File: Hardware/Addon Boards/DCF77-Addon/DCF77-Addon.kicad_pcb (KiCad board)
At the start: 2 copper layers, 79 x 40.3 mm, 11 parts, among them J1 EXT, J4 EXT, J5 I2C_ext, J6 Prog, J8 GND, SW1 RST, SW2 SW_Plus, SW3 SW_Menu, SW4 SW_Minus

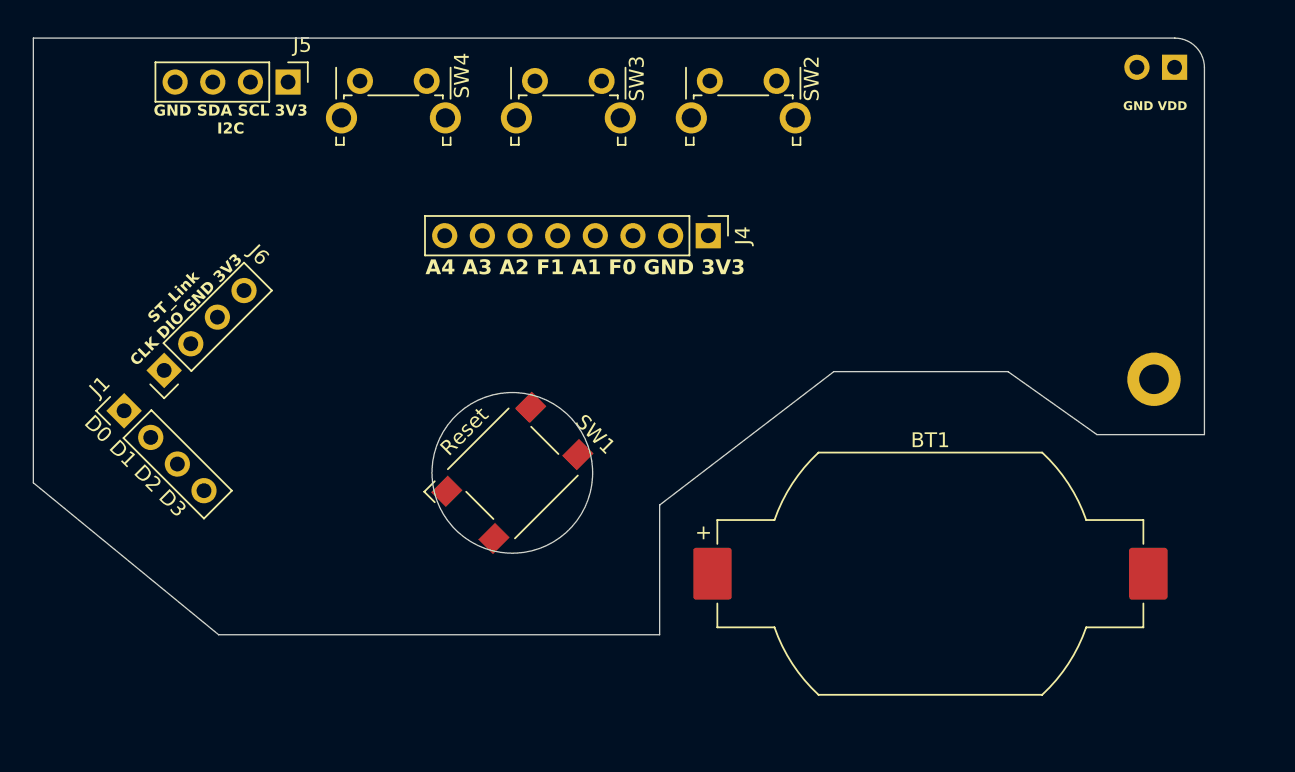
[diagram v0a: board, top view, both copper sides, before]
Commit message: Version bump 2.2.0 -> new regulator and id system
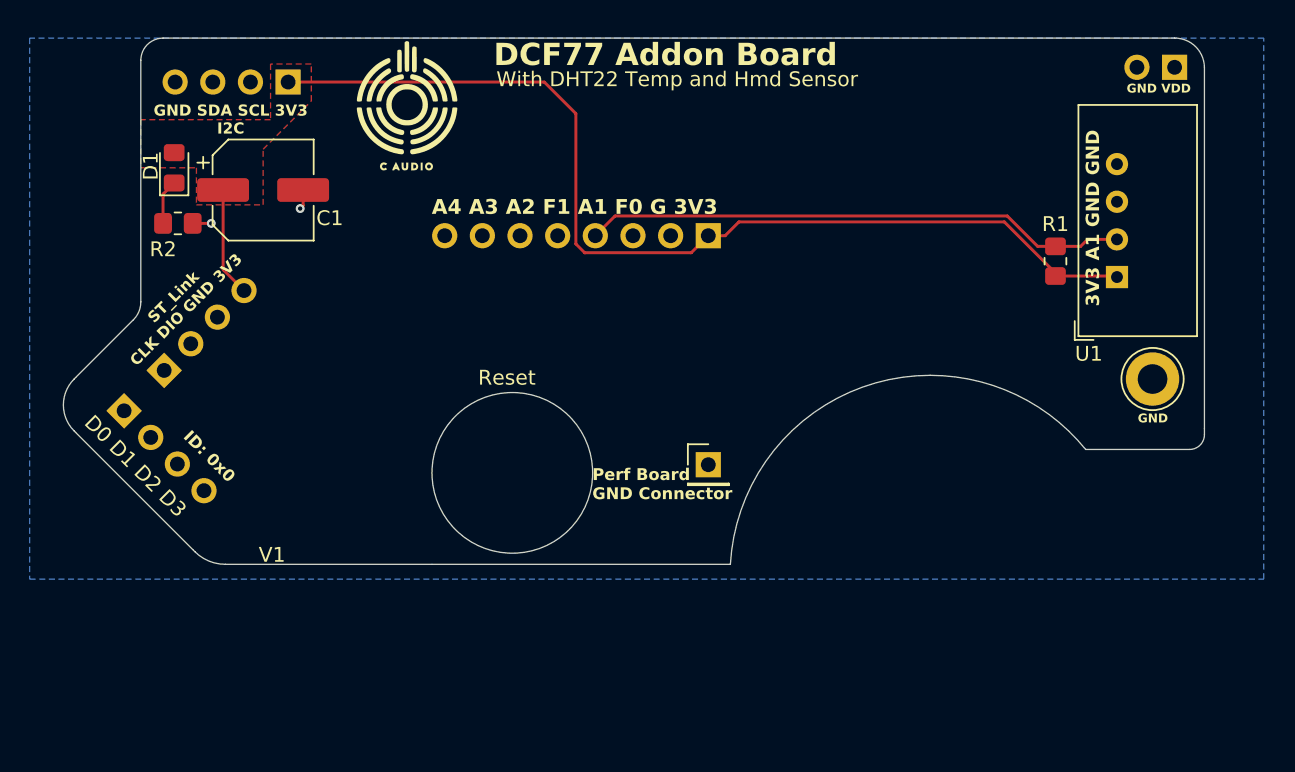
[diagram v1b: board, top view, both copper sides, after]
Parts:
- removed ?: , 
- removed BT1: Coin Cell, Battery:BatteryHolder_Renata_SMTU2032-LF_1x2032
- removed SW1: RST, Button_Switch_SMD:SW_SPST_Omron_B3FS-100xP
- removed SW2: SW_Plus, Button_Switch_THT:SW_Tactile_SPST_Angled_PTS645Vx31-2LFS
- removed SW3: SW_Menu, Button_Switch_THT:SW_Tactile_SPST_Angled_PTS645Vx31-2LFS
- removed SW4: SW_Minus, Button_Switch_THT:SW_Tactile_SPST_Angled_PTS645Vx31-2LFS
- added C1: 100u 16V, Capacitor_SMD:CP_Elec_6.3x7.7, F.Cu at (155.8, 62.8)
- added D1: LED_grn, LED_SMD:LED_0805_2012Metric_Pad1.15x1.40mm_HandSolder, F.Cu at (149.8, 61.2)
- added G***: LOGO, Logos:C Audio Logo 15mm, F.Cu at (165.5, 57.0)
- added H1: GND, TestPoint:TestPoint_Loop_D3.80mm_Drill2.0mm, F.Cu at (215.8, 75.5)
- added J2: Addon_Conn, Connector_PinHeader_2.54mm:PinHeader_1x01_P2.54mm_Vertical, F.Cu at (185.8, 81.3)
- added R1: 4k7, Resistor_SMD:R_0805_2012Metric_Pad1.20x1.40mm_HandSolder, F.Cu at (209.2, 67.5)
- added R2: 4k7, Resistor_SMD:R_0805_2012Metric_Pad1.20x1.40mm_HandSolder, F.Cu at (150.0, 65.0)
- added REF**: KiCad-Logo2_5mm_SilkScreen, Symbol:KiCad-Logo2_5mm_SilkScreen, B.Cu at (209.0, 64.5)
- added U1: AM2302, Sensor:ASAIR_AM2302_P2.54mm_Vertical, F.Cu at (213.3, 68.6)
- J1: value EXT -> Misc-PortD; footprint Connector_PinHeader_2.54mm:PinHeader_1x04_P2.54mm_Vertical -> Connector_PinSocket_2.54mm:PinSocket_1x04_P2.54mm_Vertical; moved to B.Cu
- J4: value EXT -> Misc-PortA; footprint Connector_PinHeader_2.54mm:PinHeader_1x08_P2.54mm_Vertical -> Connector_PinSocket_2.54mm:PinSocket_1x08_P2.54mm_Vertical; moved to B.Cu
- J5: value I2C_ext -> I2C; footprint Connector_PinHeader_2.54mm:PinHeader_1x04_P2.54mm_Vertical -> Connector_PinSocket_2.54mm:PinSocket_1x04_P2.54mm_Vertical; moved to B.Cu
- J6: value Prog -> ST-Link; footprint Connector_PinHeader_2.54mm:PinHeader_1x04_P2.54mm_Vertical -> Connector_PinSocket_2.54mm:PinSocket_1x04_P2.54mm_Vertical; moved to B.Cu
- J8: value GND -> VDD
- turned J1 to -135 degrees
- turned J4 to 90 degrees
- turned J5 to 90 degrees
- turned J6 to -45 degrees
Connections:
- net /PA2 renamed /A2
- net /PA3 renamed /A3
- net /PA4 renamed /A4
- net /PD0 renamed /D0
- net /PD1 renamed /D1
- J1 pad 3: /PD2 -> GND
- J1 pad 4: /PD3 -> GND
- J4 pad 4: /PA1 -> /A1
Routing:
- net +3V3: track 0.00 -> 75.7 mm
- net /A1: track 0.00 -> 36.8 mm
- net Net-(D1-K): track 0.00 -> 3.04 mm
- net GND: track 0.00 -> 2.58 mm, vias 0 -> 2
- added copper zone on F.Cu, net +3V3
- added copper zone on B.Cu, net GND
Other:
- board size 79 x 40.3 mm -> 77 x 35.5 mm
- board text added: "3V3 A1 GND GND"
- board text added: "A4 A3 A2 F1 A1 F0 G 3V3"
- board text added: "DCF77 Addon Board"
- board text added: "GND"
- board text added: "ID: 0x0"
- board text added: "Perf Board GND Connector"
- board text added: "Position von Antenne"
- board text added: "V1"
- board text added: "With DHT22 Temp and Hmd Sensor"
- board text removed: "A4 A3 A2 F1 A1 F0 GND 3V3"

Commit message: finalized DCF77 board and updated 3D pictures
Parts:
- removed the G*** at (165.5, 57.0)
- removed R1: 4k7, Resistor_SMD:R_0805_2012Metric_Pad1.20x1.40mm_HandSolder
- removed REF**: KiCad-Logo2_5mm_SilkScreen, Symbol:KiCad-Logo2_5mm_SilkScreen
- added C2: 100n, Capacitor_SMD:C_0805_2012Metric_Pad1.18x1.45mm_HandSolder, F.Cu at (164.1, 59.1)
- added G***: LOGO, Logos:C Audio Logo 25mm, F.Cu at (203.7, 64.7)
- U1: value AM2302 -> HPP845E031R1; footprint Sensor:ASAIR_AM2302_P2.54mm_Vertical -> Package_DFN_QFN:Maxim_TDFN-6-1EP_3x3mm_P0.95mm_EP1.5x2.3mm
- moved U1 50.7 mm to (164.2, 56.2), turned to 0 degrees
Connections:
- U1 pad 1: +3V3 -> /SDA
- U1 pad 2: /A1 -> GND
- U1 pad 3: GND -> unconnected-(U1-NC-Pad3)
- U1 pad 4: GND -> unconnected-(U1-NC-Pad4)
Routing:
- net /A1: track 36.8 -> 0.00 mm
- net +3V3: track 75.7 -> 55.0 mm
- net /SDA: track 0.00 -> 13.5 mm
- net /SCL: track 0.00 -> 12.8 mm
- net GND: track 2.58 -> 8.84 mm, vias 2 -> 8
- added copper zone on F.Cu, net GND
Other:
- outline, holes or cut-outs redrawn
- board text added: "With HTU21 Temp and Hmd Sensor"
- board text removed: "3V3 A1 GND GND"
- board text removed: "With DHT22 Temp and Hmd Sensor"

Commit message: finalized addon board and produced fabrication outputs
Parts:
- removed the G*** at (203.7, 64.7)
- added C3: 100n, Capacitor_SMD:C_0805_2012Metric_Pad1.18x1.45mm_HandSolder, F.Cu at (211.2, 60.1)
- added D2: LED_grn, LED_SMD:LED_0805_2012Metric_Pad1.15x1.40mm_HandSolder, F.Cu at (213.4, 60.1)
- added G***: LOGO, Logos:pcbWay_logo_15mm, F.Cu at (159.6, 78.2)
- added G***: LOGO, Logos:C Audio Logo 15mm, F.Cu at (161.6, 71.1)
- added R1: 4k7, Resistor_SMD:R_0805_2012Metric_Pad1.20x1.40mm_HandSolder, F.Cu at (215.6, 60.1)
- added REF**: KiCad-Logo2_5mm_SilkScreen, Symbol:KiCad-Logo2_5mm_SilkScreen, B.Cu at (211.3, 61.4)
- added REF**: OSHW-Logo2_7.3x6mm_SilkScreen, Symbol:OSHW-Logo2_7.3x6mm_SilkScreen, B.Cu at (213.6, 68.7)
- added U2: DCF77-Module, DCF77-Module:DCF77-Module, F.Cu at (205.5, 72.2)
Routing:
- net /A2: track 0.00 -> 33.7 mm
- net +3V3: track 55.0 -> 87.6 mm
- net /A1: track 0.00 -> 24.1 mm
- net Net-(D2-K): track 0.00 -> 2.21 mm
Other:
- board size 77 x 35.5 mm -> 77 x 47.5 mm
- board text added: "DCF77 Antenna"
- board text added: "DCF77 Module"
